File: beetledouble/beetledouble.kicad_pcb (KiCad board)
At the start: 4 copper layers, 31 x 59 mm, 49 parts, among them J1 power in, J2 rxin, J4 motor_out, J5 motor_out, J6 prog connector, Q1 IRF8313PBF, Q2 IRF8313PBF, Q3 IRF8313PBF, Q4 IRF8313PBF, U1 78L12G-AB3-R, U2 DD4012SB, U3 ATtiny1614-SS, U4 NCP81155MNTXG, U5 NCP81155MNTXG, U6 NCP81155MNTXG, U7 NCP81155MNTXG

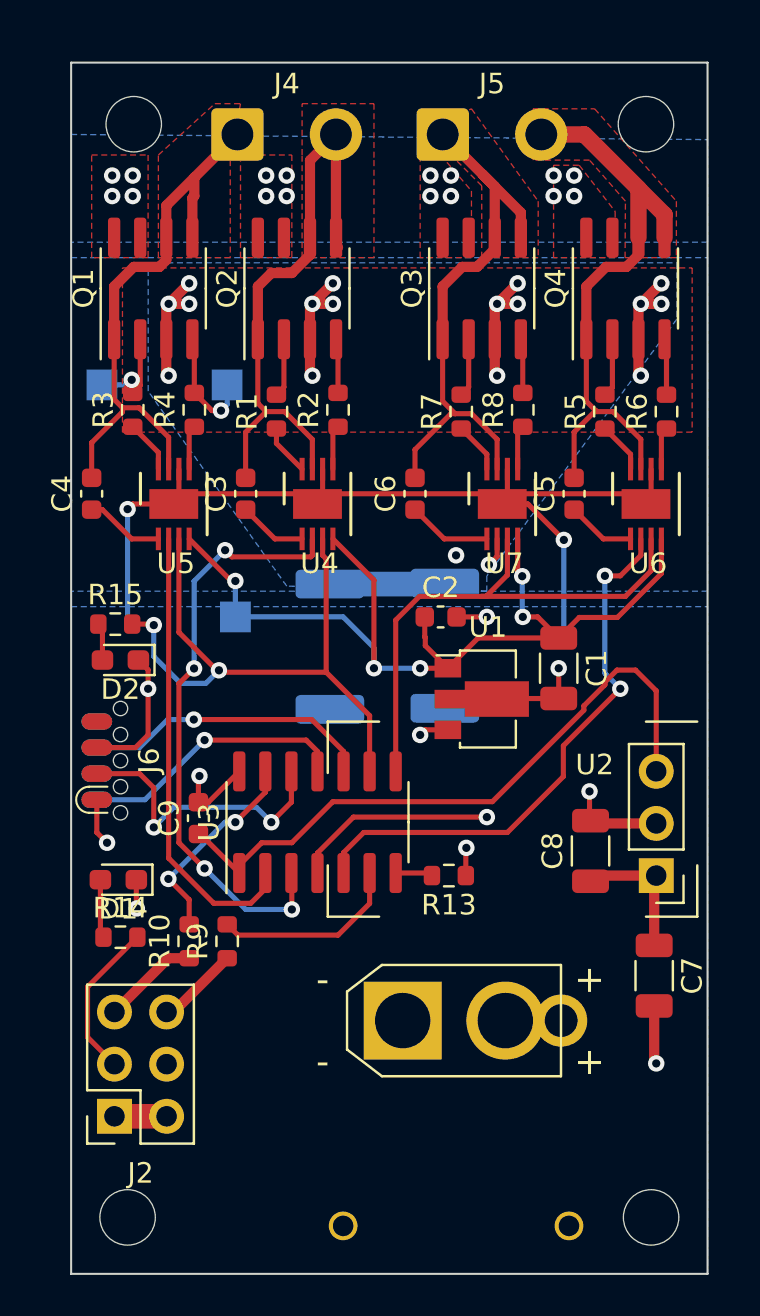
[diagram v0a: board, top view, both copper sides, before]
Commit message: Beetle double driver update with differen fets
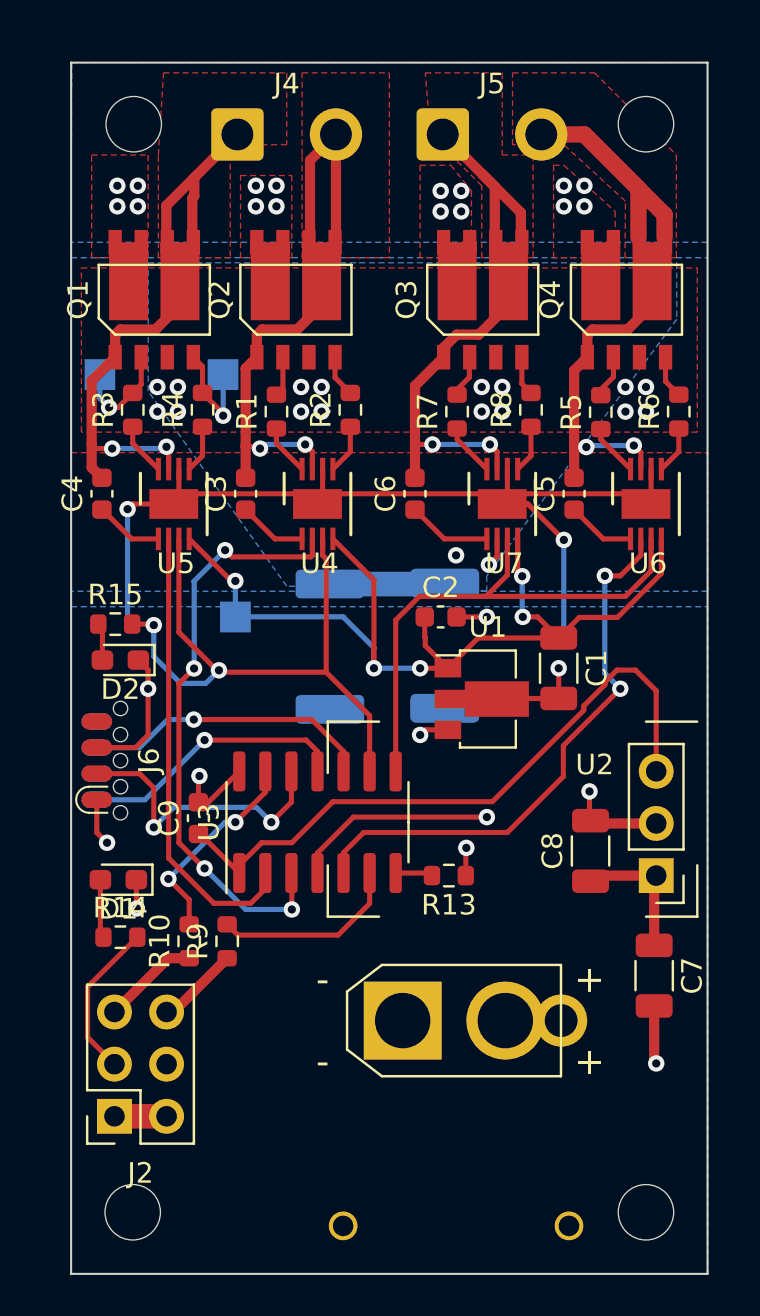
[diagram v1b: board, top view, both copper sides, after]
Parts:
- Q1, Q2, Q3, Q4: value IRF8313PBF -> IPG20N04S4-12; footprint Package_SO:SOIC-8_3.9x4.9mm_P1.27mm -> beetledouble:Infineon-PG-TDSON
- moved R2 0.60 mm to (119.6, 88.9)
- moved R6 0.60 mm to (135.6, 89.0)
- moved Q4 0.55 mm to (133.1, 83.5), turned to 0 degrees
- moved Q1 0.55 mm to (110.0, 83.5), turned to 0 degrees
- moved Q2 0.55 mm to (117.0, 83.5), turned to 0 degrees
- moved Q3 0.55 mm to (126.0, 83.5), turned to 0 degrees
- moved TP3 0.54 mm to (113.4, 87.2)
- moved TP2 0.51 mm to (107.4, 87.2)
- moved C4 0.50 mm to (107.5, 93.0)
- moved R4 0.40 mm to (112.4, 88.9)
- moved R8 0.40 mm to (128.4, 88.9)
- moved H1 0.35 mm to (134.0, 128.0)
- moved H2 0.35 mm to (109.0, 128.0)
- moved R5 0.20 mm to (131.8, 89.0)
- moved R7 0.20 mm to (124.8, 89.0)
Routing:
- net GNDSHUNT: track 45.5 -> 21.4 mm
- net /driver1/MOTORS2: track 29.3 -> 28.3 mm, vias 0 -> 2
- net /driver2/MOTORS2: track 33.0 -> 32.1 mm, vias 0 -> 2
- net /driver1/GATEH2: track 2.85 -> 1.96 mm
- net /driver2/GATEH1: track 2.85 -> 2.08 mm
- net /driver2/GATEH2: track 2.85 -> 2.10 mm
- net /driver2/GATEL1: track 2.65 -> 1.92 mm
- net /driver2/MOTORS1: track 28.3 -> 27.6 mm, vias 0 -> 2
- net /driver2/GATEL2: track 2.74 -> 2.09 mm
- net /driver1/GATEL2: track 2.65 -> 2.05 mm
- net Net-(C4-Pad1): track 3.84 -> 3.34 mm
- net /driver1/MOTORS1: track 28.1 -> 28.0 mm, vias 0 -> 2
- added copper zone on F.Cu, net GND

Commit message: Beetledouble: tweaks
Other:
- board text added: "+5v"
- board text added: "GND"
- board text added: "SIG"
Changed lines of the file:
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@@
     (property "Sheetname" "driver1")
     (attr smd)
-    (fp_text reference "C4" (at 0 -1.43 90) (layer "F.SilkS")
+    (fp_text reference "C4" (at -2.5 0 180) (layer "F.SilkS")
       (effects (font (size 1 1) (thickness 0.15)))
     )
@@
     (property "Sheetname" "driver2")
     (attr through_hole)
-    (fp_text reference "Q3" (at -3.705 0 90) (layer "F.SilkS")
+    (fp_text reference "Q3" (at -3.55 1.95 180) (layer "F.SilkS")
       (effects (font (size 1 1) (thickness 0.15)))
     )
@@
     (property "Sheetname" "driver2")
     (attr smd)
-    (fp_text reference "C6" (at 0 -1.43 90) (layer "F.SilkS")
+    (fp_text reference "C6" (at -2.5 -0.25 180) (layer "F.SilkS")
       (effects (font (size 1 1) (thickness 0.15)))
     )
@@
     (property "Sheetname" "driver1")
     (attr through_hole)
-    (fp_text reference "Q1" (at -3.705 0 90) (layer "F.SilkS")
+    (fp_text reference "Q1" (at -3.05 1.95 180) (layer "F.SilkS")
       (effects (font (size 1 1) (thickness 0.15)))
     )
@@
     (property "Sheetname" "")
     (attr smd)
-    (fp_text reference "R10" (at 0 -1.43 90) (layer "F.SilkS")
+    (fp_text reference "R10" (at 3.3 0.25 90) (layer "F.SilkS")
       (effects (font (size 1 1) (thickness 0.15)))
     )
@@
     (property "Sheetname" "")
     (attr smd)
-    (fp_text reference "D1" (at 0 -1.43) (layer "F.SilkS")
+    (fp_text reference "D1" (at 0 1.8) (layer "F.SilkS")
       (effects (font (size 1 1) (thickness 0.15)))
     )
@@
     (property "Sheetname" "driver1")
     (attr through_hole)
-    (fp_text reference "Q2" (at -3.705 0 90) (layer "F.SilkS")
+    (fp_text reference "Q2" (at -3.45 1.95 180) (layer "F.SilkS")
       (effects (font (size 1 1) (thickness 0.15)))
     )
@@
     (property "Sheetname" "driver2")
     (attr through_hole)
-    (fp_text reference "Q4" (at -3.705 0 90) (layer "F.SilkS")
+    (fp_text reference "Q4" (at -3.55 1.95 180) (layer "F.SilkS")
       (effects (font (size 1 1) (thickness 0.15)))
     )
@@
     (property "Sheetname" "")
     (attr smd)
-    (fp_text reference "D2" (at 0 -1.43) (layer "F.SilkS")
+    (fp_text reference "D2" (at -3.1 0.1) (layer "F.SilkS")
       (effects (font (size 1 1) (thickness 0.15)))
     )
@@
     (property "Sheetname" "driver1")
     (attr smd)
-    (fp_text reference "C3" (at 0 -1.43 90) (layer "F.SilkS")
+    (fp_text reference "C3" (at -2.5 0 180) (layer "F.SilkS")
       (effects (font (size 1 1) (thickness 0.15)))
     )
@@
     (property "Sheetname" "driver2")
     (attr smd)
-    (fp_text reference "C5" (at 0 -1.43 90) (layer "F.SilkS")
+    (fp_text reference "C5" (at -2.5 0 180) (layer "F.SilkS")
       (effects (font (size 1 1) (thickness 0.15)))
     )
@@
     (property "Sheetname" "")
     (attr smd)
-    (fp_text reference "U3" (at 0 -5.28 90) (layer "F.SilkS")
+    (fp_text reference "U3" (at 4.5 -2.5 180) (layer "F.SilkS")
       (effects (font (size 1 1) (thickness 0.15)))
     )
@@
     (property "Sheetname" "")
     (attr smd)
-    (fp_text reference "R9" (at 0 -1.43 90) (layer "F.SilkS")
+    (fp_text reference "R9" (at 0.3 1.9 90) (layer "F.SilkS")
       (effects (font (size 1 1) (thickness 0.15)))
     )
@@
   )
   (gr_rect (start 106 72) (end 137 131) (layer "Edge.Cuts") (width 0.1) (fill none))
+  (gr_text "+5v" (at 112.5 121) (layer "F.SilkS")
+    (effects (font (size 1 1) (thickness 0.15)) (justify left))
+  )
+  (gr_text "SIG" (at 112.5 118.5) (layer "F.SilkS")
+    (effects (font (size 1 1) (thickness 0.15)) (justify left))
+  )
+  (gr_text "GND" (at 112.5 123.5) (layer "F.SilkS")
+    (effects (font (size 1 1) (thickness 0.15)) (justify left))
+  )
   (dimension (type aligned) (layer "Dwgs.User")
     (pts (xy 106 131) (xy 137 131))

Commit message: beetledouble esc wip
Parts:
- added C10: 2.2uF, Capacitor_SMD:C_0603_1608Metric, F.Cu at (124.5, 113.2)
- J1: value power in -> XT30PW-M
- moved R13 0.14 mm to (124.5, 111.5)
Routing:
- net /ISENSE: track 1.82 -> 3.59 mm
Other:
- board text added: "+"
- board text added: "-"
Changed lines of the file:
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@@
       (effects (font (size 1 1) (thickness 0.15)))
     )
-    (fp_text value "power in" (at 2.5 4 unlocked) (layer "F.Fab")
+    (fp_text value "XT30PW-M" (at 2.5 4 unlocked) (layer "F.Fab")
       (effects (font (size 1 1) (thickness 0.15)))
     )
@@
     (pad "1" np_thru_hole circle locked (at 0 0) (size 2.7 2.7) (drill 2.7) (layers *.Cu *.Mask))
   )
+  (footprint "Capacitor_SMD:C_0603_1608Metric" (layer "F.Cu")
+    (at 124.5 113.25)
+    (descr "Capacitor SMD 0603 (1608 Metric), square (rectangular) end terminal, IPC_7351 nominal, (Body size source: IPC-SM-782 page 76, https://www.pcb-3d.com/wordpress/wp-content/uploads/ipc-sm-782a_amendment_1_and_2.pdf), generated with kicad-footprint-generator")
+    (tags "capacitor")
+    (property "LCSC" "")
+    (property "Sheetfile" "beetledouble.kicad_sch")
+    (property "Sheetname" "")
+    (attr smd)
+    (fp_text reference "C10" (at 0 -1.43) (layer "F.SilkS")
+      (effects (font (size 1 1) (thickness 0.15)))
+    )
+    (fp_text value "2.2uF" (at 0 1.43) (layer "F.Fab")
+      (effects (font (size 1 1) (thickness 0.15)))
+    )
+    (fp_text user "${REFERENCE}" (at 0 0) (layer "F.Fab")
+      (effects (font (size 0.4 0.4) (thickness 0.06)))
+    )
+    (fp_line (start -0.14058 -0.51) (end 0.14058 -0.51) (layer "F.SilkS") (width 0.12))
+    (fp_line (start -0.14058 0.51) (end 0.14058 0.51) (layer "F.SilkS") (width 0.12))
+    (fp_line (start -1.48 0.73) (end -1.48 -0.73) (layer "F.CrtYd") (width 0.05))
+    (fp_line (start 1.48 -0.73) (end 1.48 0.73) (layer "F.CrtYd") (width 0.05))
+    (fp_line (start -1.48 -0.73) (end 1.48 -0.73) (layer "F.CrtYd") (width 0.05))
+    (fp_line (start 1.48 0.73) (end -1.48 0.73) (layer "F.CrtYd") (width 0.05))
+    (fp_line (start 0.8 -0.4) (end 0.8 0.4) (layer "F.Fab") (width 0.1))
+    (fp_line (start -0.8 0.4) (end -0.8 -0.4) (layer "F.Fab") (width 0.1))
+    (fp_line (start 0.8 0.4) (end -0.8 0.4) (layer "F.Fab") (width 0.1))
+    (fp_line (start -0.8 -0.4) (end 0.8 -0.4) (layer "F.Fab") (width 0.1))
+    (pad "1" smd roundrect locked (at -0.775 0) (size 0.9 0.95) (layers "F.Cu" "F.Paste" "F.Mask") (roundrect_rratio 0.25)
+      (net 46 "/ISENSE") (pintype "passive"))
+    (pad "2" smd roundrect locked (at 0.775 0) (size 0.9 0.95) (layers "F.Cu" "F.Paste" "F.Mask") (roundrect_rratio 0.25)
+      (net 2 "GND") (pintype "passive"))
+    (model "${KICAD6_3DMODEL_DIR}/Capacitor_SMD.3dshapes/C_0603_1608Metric.wrl"
+      (offset (xyz 0 0 0))
+      (scale (xyz 1 1 1))
+      (rotate (xyz 0 0 0))
+    )
+  )
   (footprint "Resistor_SMD:R_0603_1608Metric" (layer "F.Cu")
-    (at 124.4 111.6 180)
+    (at 124.5 111.5 180)
     (descr "Resistor SMD 0603 (1608 Metric), square (rectangular) end terminal, IPC_7351 nominal, (Body size source: IPC-SM-782 page 72, https://www.pcb-3d.com/wordpress/wp-content/uploads/ipc-sm-782a_amendment_1_and_2.pdf), generated with kicad-footprint-generator")
     (tags "resistor")
@@
     (property "Sheetname" "")
     (attr through_hole)
-    (fp_text reference "U2" (at 3 5.4) (layer "F.SilkS")
+    (fp_text reference "U2" (at 6.5 3.85) (layer "F.SilkS")
       (effects (font (size 1 1) (thickness 0.15)))
     )
@@
   )
   (gr_rect (start 106 72) (end 137 131) (layer "Edge.Cuts") (width 0.1) (fill none))
+  (gr_text "-" (at 118.11 115.57) (layer "B.SilkS")
+    (effects (font (size 1.5 1.5) (thickness 0.15)))
+  )
+  (gr_text "+" (at 130.81 121.92) (layer "B.SilkS")
+    (effects (font (size 1.5 1.5) (thickness 0.15)))
+  )
+  (gr_text "+" (at 130.81 115.57) (layer "B.SilkS")
+    (effects (font (size 1.5 1.5) (thickness 0.15)))
+  )
+  (gr_text "-" (at 118.11 121.92) (layer "B.SilkS")
+    (effects (font (size 1.5 1.5) (thickness 0.15)))
+  )
   (gr_text "+5v" (at 112.5 121) (layer "F.SilkS")
     (effects (font (size 1 1) (thickness 0.15)) (justify left))
@@
   (gr_text "GND" (at 112.5 123.5) (layer "F.SilkS")
     (effects (font (size 1 1) (thickness 0.15)) (justify left))
+  )
+  (gr_text "+5v" (at 132.75 106.5) (layer "F.SilkS")
+    (effects (font (size 1 1) (thickness 0.15)) (justify right))
   )
   (dimension (type aligned) (layer "Dwgs.User")
@@
   (segment (start 110.98 118.245) (end 113.6 115.625) (width 0.5) (layer "F.Cu") (net 45))
   (segment (start 110.65 118.245) (end 110.98 118.245) (width 0.5) (layer "F.Cu") (net 45))
+  (segment (start 123.675 113.2) (end 123.725 113.25) (width 0.25) (layer "F.Cu") (net 46))
+  (segment (start 123.675 111.5) (end 123.675 113.2) (width 0.25) (layer "F.Cu") (net 46))
   (segment (start 121.81 111.475) (end 123.45 111.475) (width 0.25) (layer "F.Cu") (net 46))
   (segment (start 123.45 111.475) (end 123.575 111.6) (width 0.25) (layer "F.Cu") (net 46))

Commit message: Beetle esc
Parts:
- added D3: B5819W, Diode_SMD:D_SOD-123, F.Cu at (111.0, 97.0)
- added D4: B5819W, Diode_SMD:D_SOD-123, F.Cu at (118.0, 97.0)
- added D5: B5819W, Diode_SMD:D_SOD-123, F.Cu at (125.4, 97.0)
- added D6: B5819W, Diode_SMD:D_SOD-123, F.Cu at (132.4, 97.0)
- Q1, Q2, Q3, Q4: value IPG20N04S4-12 -> AON6884
- U4, U5, U6, U7: value NCP81155MNTXG -> ADP3110A
- moved U6 8.67 mm to (125.4, 92.5)
- moved U4 7.07 mm to (111.0, 92.5)
- moved U5 7.07 mm to (118.0, 92.5)
- moved U7 5.48 mm to (132.4, 92.5)
- moved R5 1.53 mm to (130.7, 88.0)
- moved Q4 1.53 mm to (131.9, 82.5)
- moved Q3 1.53 mm to (124.9, 82.5)
- moved R7 1.53 mm to (123.7, 88.0)
- moved R8 1.53 mm to (127.3, 87.9)
- moved R6 1.53 mm to (134.5, 88.0)
- moved C5 1.49 mm to (121.6, 92.0)
- moved C6 1.49 mm to (129.4, 92.0)
- moved H4 1.14 mm to (108.5, 74.0)
- moved H3 1.12 mm to (134.5, 74.0)
- moved C2 1.11 mm to (122.9, 99.0)
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- renumbered C4 to C3, C3 to C4, C6 to C5, C5 to C6
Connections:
- C3 pad 1: Net-(C4-Pad1) -> /driver1/BOOST1
- C4 pad 1: Net-(C3-Pad1) -> /driver1/BOOST2
- C5 pad 1: Net-(C6-Pad1) -> /driver2/BOOST1
- C6 pad 1: Net-(C5-Pad1) -> /driver2/BOOST2
- U4 pad 1: Net-(C3-Pad1) -> /driver1/BOOST1
- U4 pad 2: MOTORR_1 -> MOTORF_1
- U4 pad 5: /driver1/MOTORL2 -> /driver1/MOTORL1
- U4 pad 7: /driver1/MOTORS2 -> /driver1/MOTORS1
- U4 pad 8: /driver1/MOTORH2 -> /driver1/MOTORH1
- U5 pad 1: Net-(C4-Pad1) -> /driver1/BOOST2
- U5 pad 2: MOTORF_1 -> MOTORR_1
- U5 pad 5: /driver1/MOTORL1 -> /driver1/MOTORL2
- U5 pad 7: /driver1/MOTORS1 -> /driver1/MOTORS2
- U5 pad 8: /driver1/MOTORH1 -> /driver1/MOTORH2
- U6 pad 1: Net-(C5-Pad1) -> /driver2/BOOST1
- U6 pad 2: MOTORR_2 -> MOTORF_2
- U6 pad 5: /driver2/MOTORL2 -> /driver2/MOTORL1
- U6 pad 7: /driver2/MOTORS2 -> /driver2/MOTORS1
- U6 pad 8: /driver2/MOTORH2 -> /driver2/MOTORH1
- U7 pad 1: Net-(C6-Pad1) -> /driver2/BOOST2
- U7 pad 2: MOTORF_2 -> MOTORR_2
- U7 pad 5: /driver2/MOTORL1 -> /driver2/MOTORL2
- U7 pad 7: /driver2/MOTORS1 -> /driver2/MOTORS2
- U7 pad 8: /driver2/MOTORH1 -> /driver2/MOTORH2
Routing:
- net GND: track 77.6 -> 59.9 mm, vias 9 -> 7
- net /driver2/MOTORS2: track 32.1 -> 16.5 mm
- net /driver1/MOTORS2: track 28.3 -> 16.1 mm
- net /driver1/MOTORS1: track 28.0 -> 16.2 mm
- net /driver2/MOTORS1: track 27.6 -> 16.7 mm
- net /driver2/BOOST1: track 0.00 -> 6.67 mm
- net /driver1/BOOST2: track 0.00 -> 6.20 mm
- net /driver1/BOOST1: track 0.00 -> 6.16 mm
- net /driver2/BOOST2: track 0.00 -> 5.67 mm
- net Net-(C6-Pad1): track 4.09 -> 0.00 mm
- net Net-(C4-Pad1): track 3.34 -> 0.00 mm
- net Net-(C3-Pad1): track 3.34 -> 0.00 mm
- net Net-(C5-Pad1): track 3.34 -> 0.00 mm
- net MOTORF_2: track 24.3 -> 27.4 mm
- net MOTOR_ENABLE_1: track 31.5 -> 28.6 mm, vias 2 -> 5
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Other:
- board size 31 x 59 mm -> 32 x 60 mm

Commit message: Beetledouble ESC
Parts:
- added C11: 10uF 50V, Capacitor_SMD:C_1206_3216Metric, B.Cu at (108.5, 81.5)
- added C12: 10uF 50V, Capacitor_SMD:C_1206_3216Metric, B.Cu at (115.5, 81.5)
- added C13: DNP, Capacitor_SMD:C_1206_3216Metric, B.Cu at (112.0, 81.5)
- added C14: 10uF 50V, Capacitor_SMD:C_1206_3216Metric, B.Cu at (122.5, 81.5)
- added C15: 10uF 50V, Capacitor_SMD:C_1206_3216Metric, B.Cu at (129.5, 81.5)
- added C16: DNP, Capacitor_SMD:C_1206_3216Metric, B.Cu at (126.0, 81.5)
- added C17: DNP, Capacitor_SMD:C_1206_3216Metric, B.Cu at (119.0, 81.5)
- added C18: DNP, Capacitor_SMD:C_1206_3216Metric, B.Cu at (133.0, 81.5)
- C10: value 2.2uF -> 2.2uF 50V

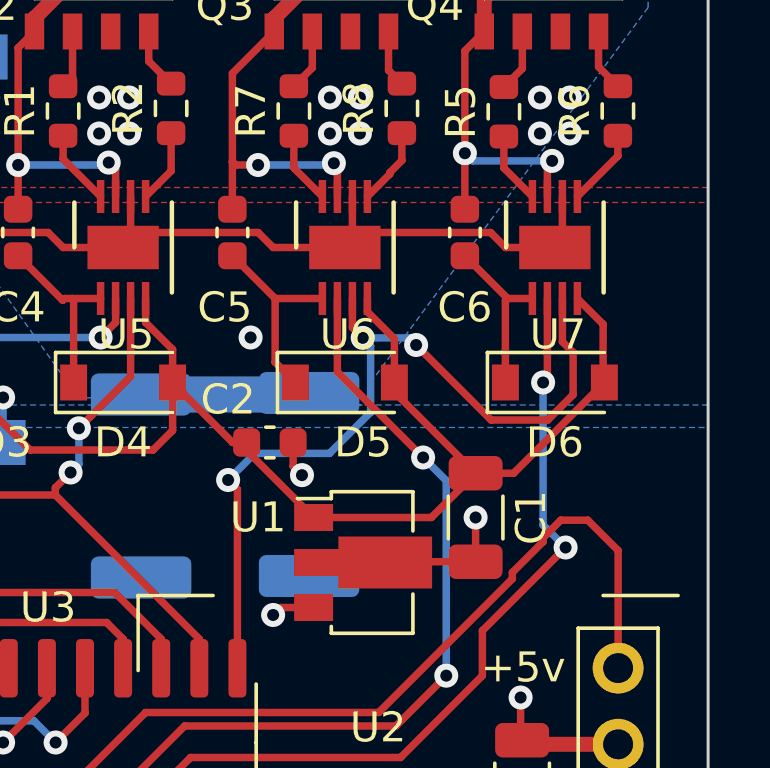
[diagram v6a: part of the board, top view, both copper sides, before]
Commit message: fix capcitor lcsc id, change driver chip to NCP81155
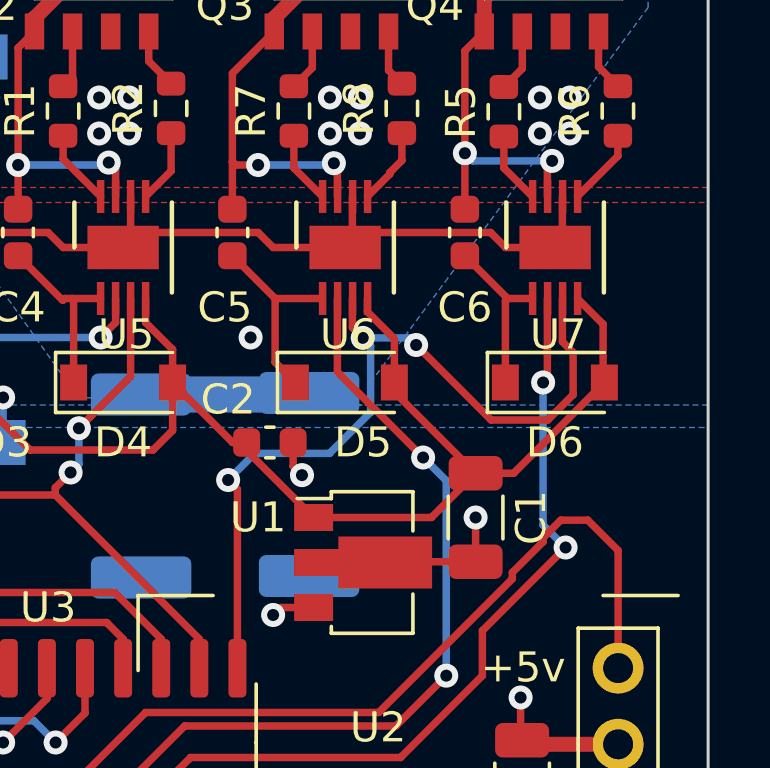
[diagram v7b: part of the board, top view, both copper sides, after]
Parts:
- U4, U5, U6, U7: value ADP3110A -> NCP81155MN

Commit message: Updates
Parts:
- added JP1: CONFIG1, Jumper:SolderJumper-2_P1.3mm_Open_TrianglePad1.0x1.5mm, B.Cu at (107.0, 114.3)
- J4, J5: footprint Connector_Wire:SolderWire-0.75sqmm_1x02_P4.8mm_D1.25mm_OD2.3mm -> beetledouble:beetlemotor
- Q1, Q2, Q3, Q4: value AON6884 -> SE3082G
- moved J4 0.78 mm to (113.5, 74.0)
- moved J5 0.78 mm to (123.5, 74.0)
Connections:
- J6 pad 2: RXDEBUG -> unconnected-(J6-Pad2)
- U3 pad 12: RXDEBUG -> CONFIG1
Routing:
- net RXDEBUG: track 14.3 -> 0.00 mm, vias 2 -> 0
- net CONFIG1: track 0.00 -> 13.8 mm, vias 0 -> 1
